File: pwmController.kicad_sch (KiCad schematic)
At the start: 0 parts

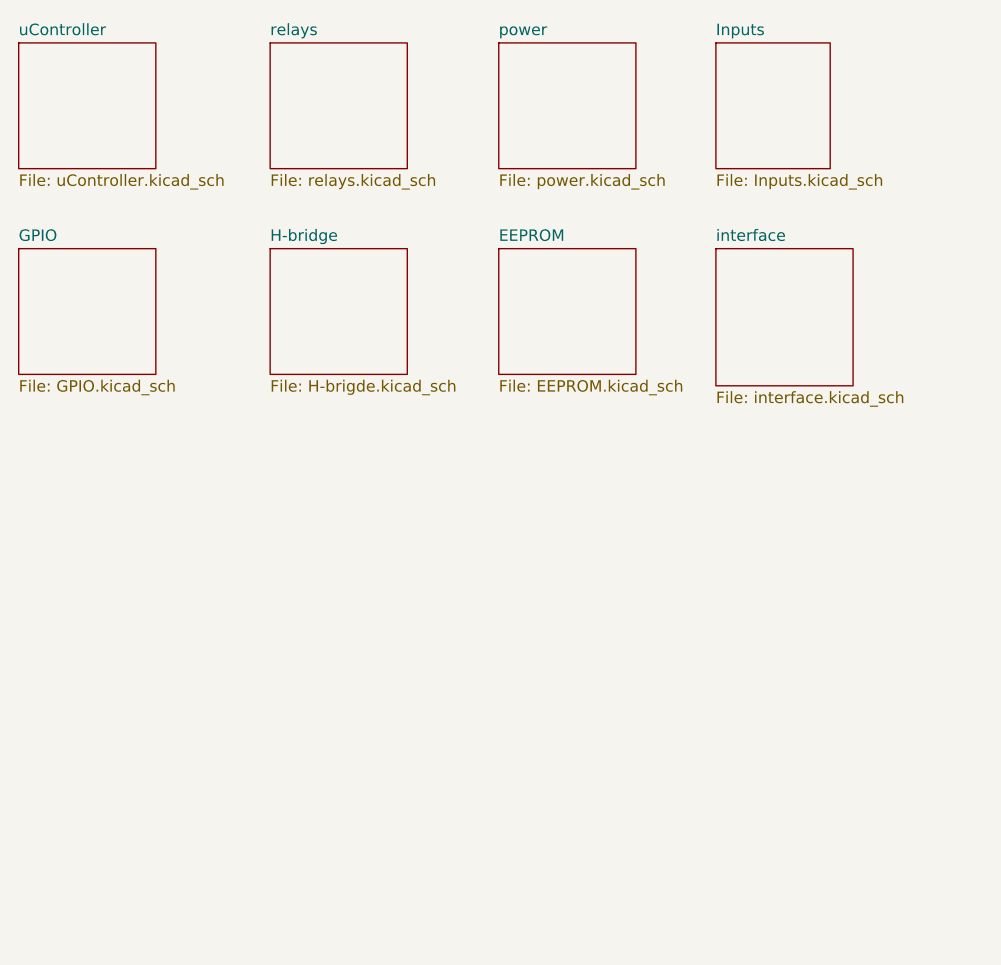
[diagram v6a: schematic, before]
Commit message: altered the code drastically and made a new PCB. PCB is still much work.
I finally fixed that issue where loco functions and speed were not serviced to the multimaus clients.
The Nx code also has been succesfully tested using the monitor.
MCP bug also has been solded. The bug was in assembleIO.py
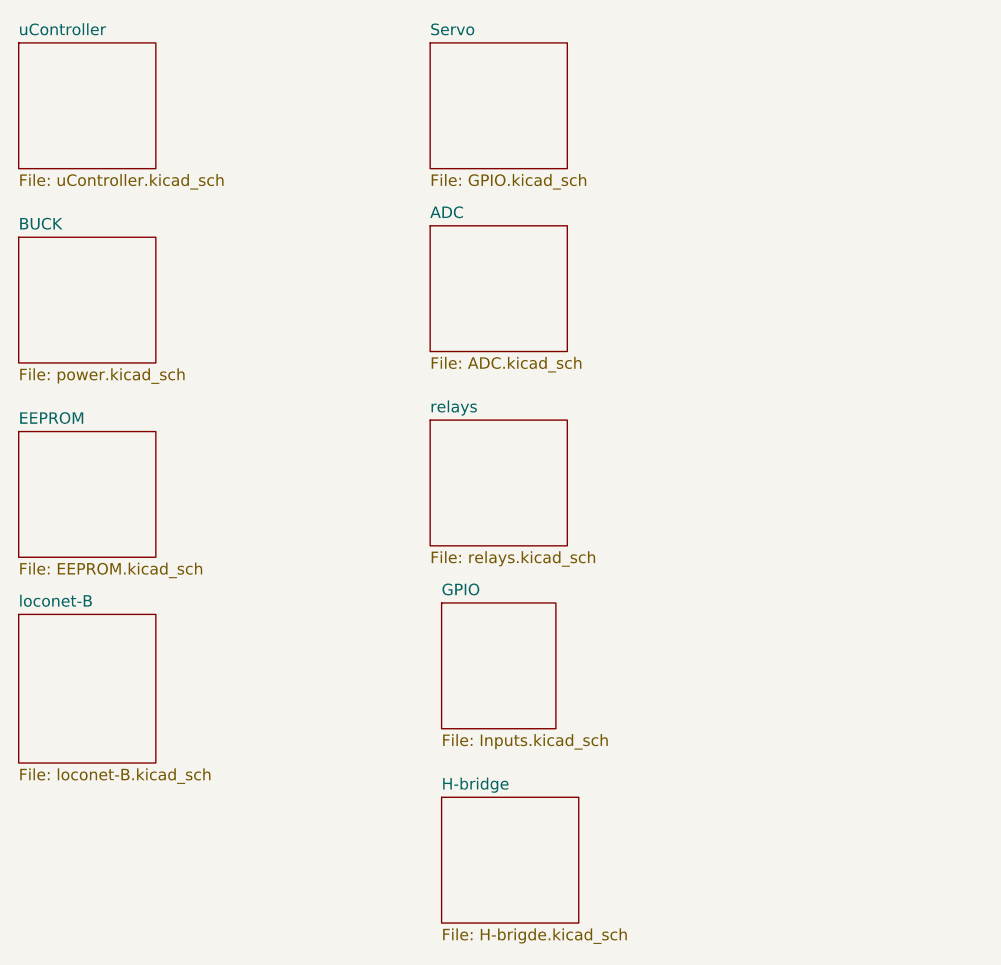
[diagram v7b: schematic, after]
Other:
- sheet power renamed BUCK
- removed sheet Inputs
- removed sheet interface
- added sheet ADC (ADC.kicad_sch)
- added sheet Servo (GPIO.kicad_sch)
- added sheet loconet-B (loconet-B.kicad_sch)
- sheet GPIO: file GPIO.kicad_sch -> Inputs.kicad_sch
